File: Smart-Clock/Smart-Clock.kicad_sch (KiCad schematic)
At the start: 15 parts, among them SW1 RotaryEncoder_Switch, SW2 SW_SPDT, U1 ESP32-WROOM-32D, U2 RC1602A

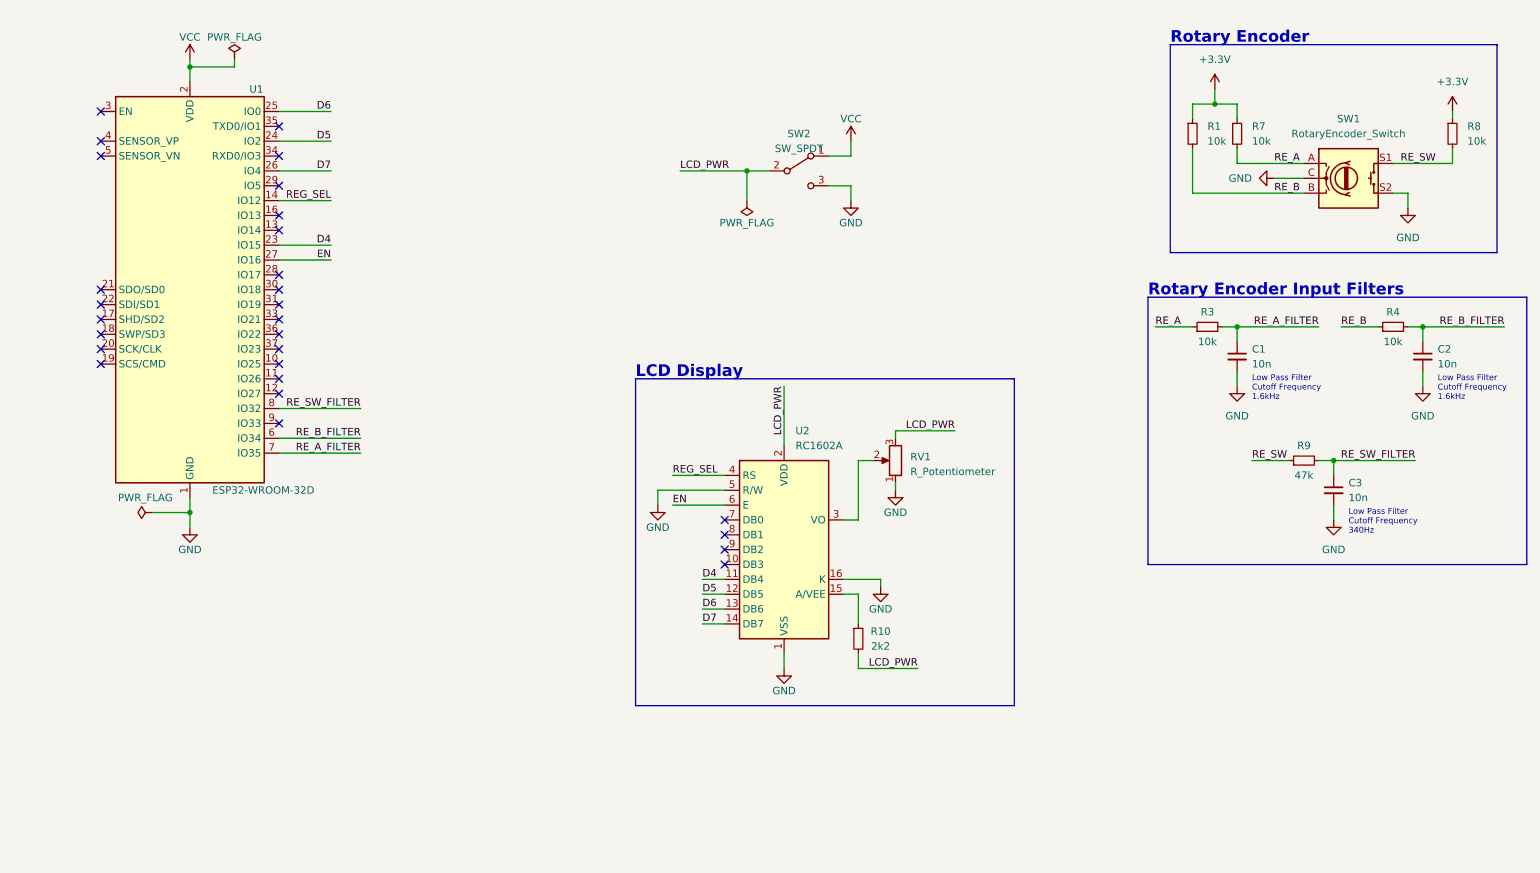
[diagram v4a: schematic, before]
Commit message: ESP32 connections updated, usb-uart added and power circuit added.
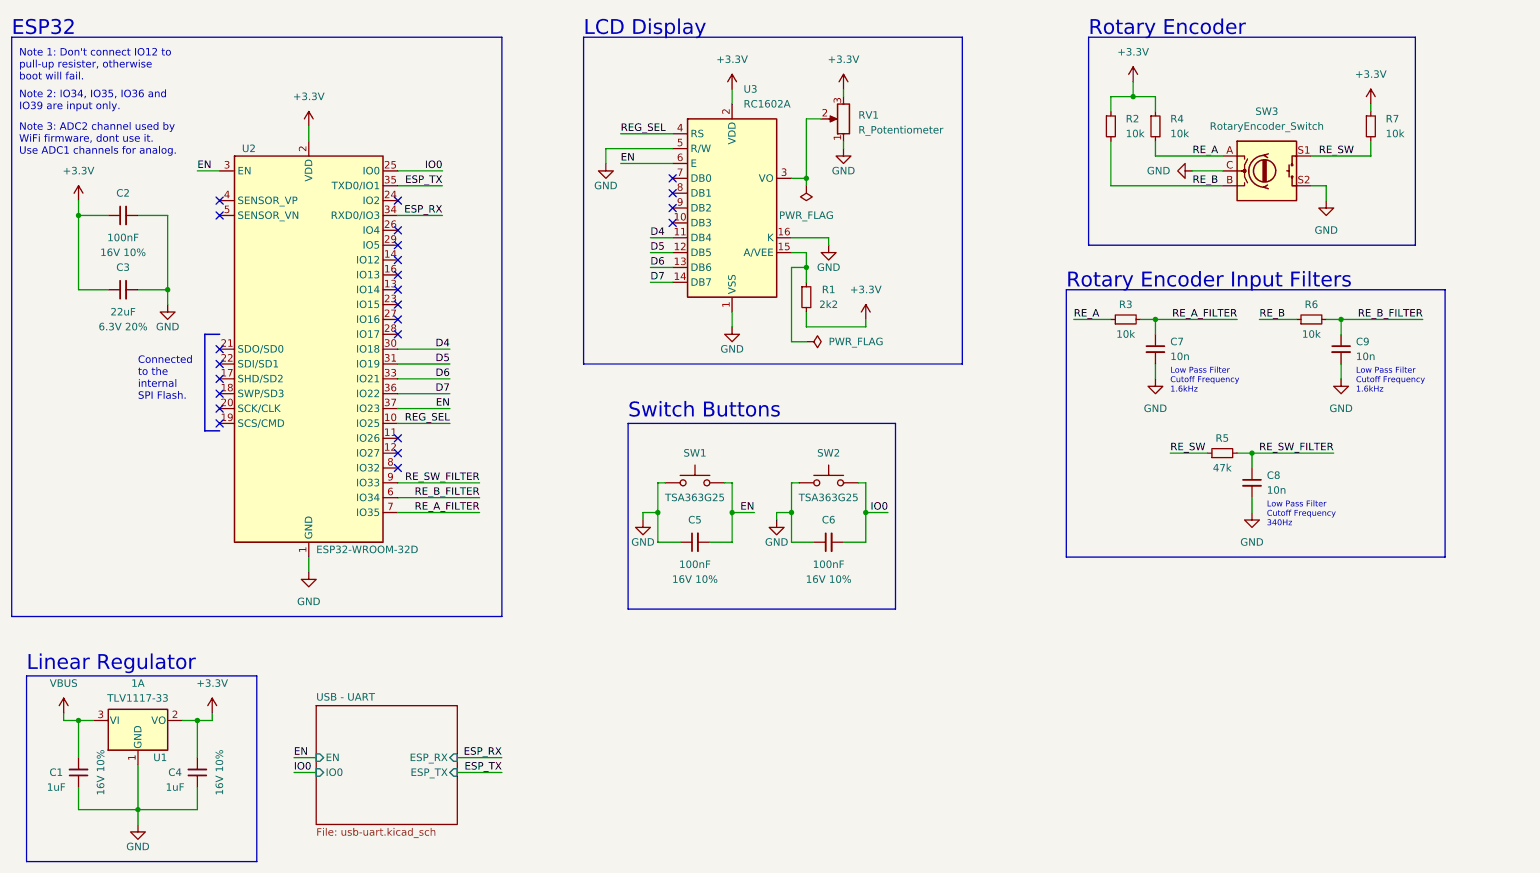
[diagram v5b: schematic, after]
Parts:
- removed SW2: SW_SPDT, Button_Switch_THT:SW_E-Switch_EG1224_SPDT_Angled, symbol Switch:SW_SPDT
- removed U1: ESP32-WROOM-32D, RF_Module:ESP32-WROOM-32D, symbol RF_Module:ESP32-WROOM-32D
- added C1, C4: 1uF, Capacitor_SMD:C_0603_1608Metric, symbol Device:C_Small
- added C2, C5, C6: 100nF, Capacitor_SMD:C_0402_1005Metric, symbol Device:C_Small
- added C3: 22uF, Capacitor_SMD:C_0603_1608Metric, symbol Device:C_Small
- added SW1, SW2: TSA363G25, Button_Switch_SMD:SW_SPST_CK_RS282G05A3, symbol Switch:SW_Push
- added U1: TLV1117-33, Package_TO_SOT_SMD:SOT-223-3_TabPin2, symbol Regulator_Linear:TLV1117-33
- added U2: ESP32-WROOM-32D, RF_Module:ESP32-WROOM-32, symbol RF_Module:ESP32-WROOM-32D
- renumbered C1 to C7, C3 to C8, C2 to C9, R10 to R1, R1 to R2, R7 to R4, R9 to R5, R4 to R6, R8 to R7, SW1 to SW3, U2 to U3
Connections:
- net LCD_PWR is gone; now on net +3.3V: R1.2, RV1.3, U3.2 (VDD)
- net +3.3V: now also C2.1, C3.1, C4.2, U1.2 (VO), U2.2 (VDD)
- net D4: now also U2.30 (IO18)
- net D5: now also U2.31 (IO19)
- net D6: now also U2.33 (IO21)
- net D7: now also U2.36 (IO22)
- net EN: now also C5.2, SW1.2, U2.3 (EN), U2.37 (IO23)
- net GND: now also C1.1, C2.2, C3.2, C4.1, C5.1, C6.1, SW1.1, SW2.1, U1.1 (GND), U2.1 (GND), U2.15 (GND), U2.38 (GND), U2.39 (GND)
- net REG_SEL: now also U2.10 (IO25)
- net RE_A_FILTER: now also U2.7 (IO35)
- net RE_B_FILTER: now also U2.6 (IO34)
- net RE_SW_FILTER: now also U2.9 (IO33)
- new net ESP_RX: U2.34 (RXD0/IO3)
- new net ESP_TX: U2.35 (TXD0/IO1)
- new net IO0: C6.2, SW2.2, U2.25 (IO0)
- new net VBUS: C1.2, U1.3 (VI)
- no-connect marks 28 -> 24
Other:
- added sheet USB - UART (usb-uart.kicad_sch)
- note added: "Connected to the internal SPI Flash."
- note added: "ESP32"
- note added: "Linear Regulator"
- note added: "Note 1: Don't connect IO12 to pull-up resister, otherwise boot will fail."
- note added: "Note 2: IO34, IO35, IO36 and IO39 are input only."
- note added: "Note 3: ADC2 channel used by WiFi firmware, dont use it. Use ADC1 channels for analog."
- note added: "Switch Buttons"
- moved on the sheet: C7, C8, C9, R1, R2, R3, R4, R5, R6, R7, RV1, SW3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

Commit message: Added RGB status led.
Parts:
- added D5: WS2812B, LED_SMD:LED_WS2812B_PLCC4_5.0x5.0mm_P3.2mm, symbol LED:WS2812B
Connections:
- net GND: now also D5.3 (VSS)
- net VBUS: now also D5.1 (VDD)
- net RGB: now reaches U2.29 (IO5)
- net RGB: now also D5.4 (DIN)
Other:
- note added: "RGB Status LED"
- moved on the sheet: C1, C4, U1
